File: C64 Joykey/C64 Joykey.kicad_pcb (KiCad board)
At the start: 2 copper layers, 99.7 x 74.9 mm, 30 parts, among them J1 Port_1, J2 Port_2, M1 Mounting, M2 Mounting, M3 Mounting, M4 Mounting, SW1 FIRE1, SW2 FIRE2, SW3 FIRE3, SW4 UP, SW5 DOWN, SW6 LEFT, SW7 RIGHT, SW8 RESET

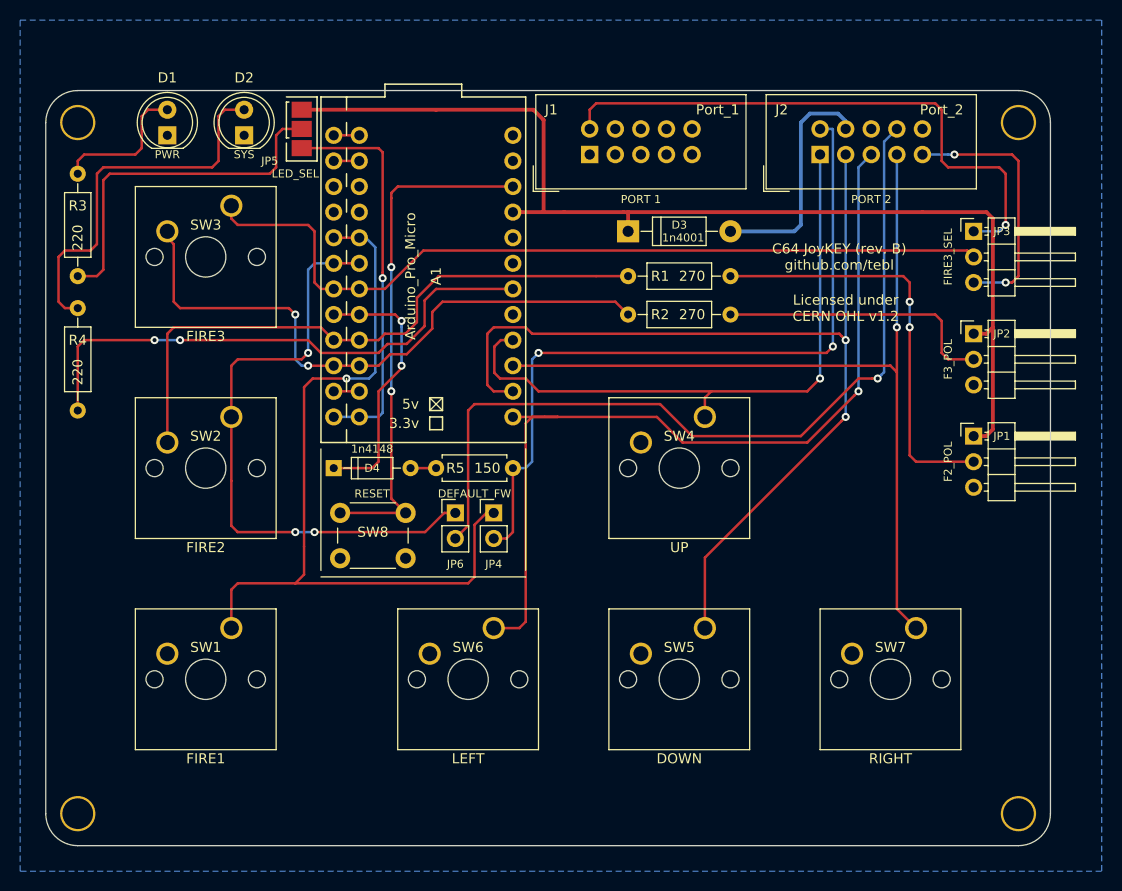
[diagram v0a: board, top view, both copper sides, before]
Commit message: Underglow LEDs added
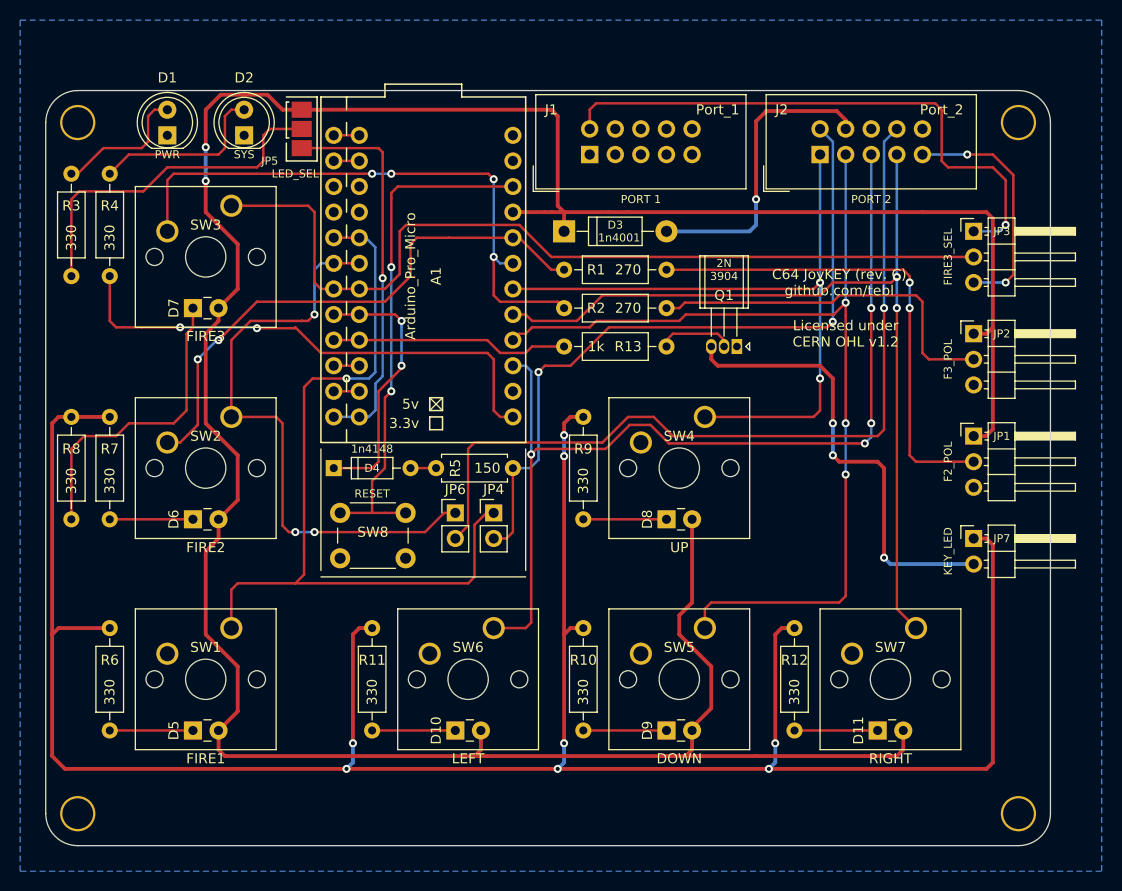
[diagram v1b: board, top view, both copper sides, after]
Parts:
- added D10: LED, LED_THT:LED_Rectangular_W3.0mm_H2.0mm, F.Cu at (181.6, 146.1)
- added D11: LED, LED_THT:LED_Rectangular_W3.0mm_H2.0mm, F.Cu at (223.5, 146.1)
- added D5: LED, LED_THT:LED_Rectangular_W3.0mm_H2.0mm, F.Cu at (155.6, 146.1)
- added D6: LED, LED_THT:LED_Rectangular_W3.0mm_H2.0mm, F.Cu at (155.6, 125.1)
- added D7: LED, LED_THT:LED_Rectangular_W3.0mm_H2.0mm, F.Cu at (155.6, 104.1)
- added D8: LED, LED_THT:LED_Rectangular_W3.0mm_H2.0mm, F.Cu at (202.6, 125.1)
- added D9: LED, LED_THT:LED_Rectangular_W3.0mm_H2.0mm, F.Cu at (202.6, 146.1)
- added JP7: KEY_LED, Connector_PinHeader_2.54mm:PinHeader_1x02_P2.54mm_Horizontal, F.Cu at (233.0, 127.0)
- added Q1: 2N3904, Package_TO_SOT_THT:TO-92_Inline_W4.0mm_Horizontal_FlatSideDown, F.Cu at (209.6, 108.0)
- added R10: 330, Resistor_THT:R_Axial_DIN0207_L6.3mm_D2.5mm_P10.16mm_Horizontal, F.Cu at (194.3, 146.1)
- added R11: 330, Resistor_THT:R_Axial_DIN0207_L6.3mm_D2.5mm_P10.16mm_Horizontal, F.Cu at (173.4, 146.1)
- added R12: 330, Resistor_THT:R_Axial_DIN0207_L6.3mm_D2.5mm_P10.16mm_Horizontal, F.Cu at (215.3, 146.1)
- added R13: 1k, Resistor_THT:R_Axial_DIN0207_L6.3mm_D2.5mm_P10.16mm_Horizontal, F.Cu at (202.6, 108.0)
- added R6: 330, Resistor_THT:R_Axial_DIN0207_L6.3mm_D2.5mm_P10.16mm_Horizontal, F.Cu at (147.3, 146.1)
- added R7: 330, Resistor_THT:R_Axial_DIN0207_L6.3mm_D2.5mm_P10.16mm_Horizontal, F.Cu at (147.3, 125.1)
- added R8: 330, Resistor_THT:R_Axial_DIN0207_L6.3mm_D2.5mm_P10.16mm_Horizontal, F.Cu at (143.5, 125.1)
- added R9: 330, Resistor_THT:R_Axial_DIN0207_L6.3mm_D2.5mm_P10.16mm_Horizontal, F.Cu at (194.3, 125.1)
- JP4, JP6: footprint Pin_Headers:Pin_Header_Straight_1x02_Pitch2.54mm -> Connector_PinHeader_2.54mm:PinHeader_1x02_P2.54mm_Vertical
- R1, R2: footprint Resistors_THT:R_Axial_DIN0207_L6.3mm_D2.5mm_P10.16mm_Horizontal -> Resistor_THT:R_Axial_DIN0207_L6.3mm_D2.5mm_P10.16mm_Horizontal
- R3, R4: value 220 -> 330; footprint Resistors_THT:R_Axial_DIN0207_L6.3mm_D2.5mm_P10.16mm_Horizontal -> Resistor_THT:R_Axial_DIN0207_L6.3mm_D2.5mm_P10.16mm_Horizontal
- R5: footprint Resistors_THT:R_Axial_DIN0207_L6.3mm_D2.5mm_P7.62mm_Horizontal -> Resistor_THT:R_Axial_DIN0207_L6.3mm_D2.5mm_P7.62mm_Horizontal
- moved R4 13.7 mm to (147.3, 90.8)
- moved R1 6.38 mm to (192.4, 100.3)
- moved R2 6.38 mm to (192.4, 104.1)
- moved D3 6.35 mm to (192.4, 96.5)
- moved R3 0.64 mm to (143.5, 90.8)
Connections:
- A1 pad 10: /FIRE3_POL -> Net-(A1-Pad10)
- A1 pad 13: P2_LEFT -> Net-(A1-Pad13)
- A1 pad 14: P2_DOWN -> Net-(A1-Pad14)
- A1 pad 15: P2_RIGHT -> P2_LEFT
- A1 pad 16: P2_UP -> P2_DOWN
- A1 pad 17: (no net) -> P2_RIGHT
- A1 pad 18: Net-(A1-Pad18) -> P2_UP
- A1 pad 19: (no net) -> FIRE3_POL
- A1 pad 20: (no net) -> FIRE2_POL
- A1 pad 24: (no net) -> Net-(A1-Pad24)
- A1 pad 9: /FIRE2_POL -> Net-(A1-Pad9)
- J1 pad 1: (no net) -> Net-(J1-Pad1)
- J1 pad 10: (no net) -> Net-(J1-Pad10)
- J1 pad 2: (no net) -> Net-(J1-Pad2)
- J1 pad 3: (no net) -> Net-(J1-Pad3)
- J1 pad 4: (no net) -> Net-(J1-Pad4)
- J1 pad 5: (no net) -> Net-(J1-Pad5)
- J1 pad 7: (no net) -> Net-(J1-Pad7)
- J1 pad 9: (no net) -> Net-(J1-Pad9)
- J2 pad 10: (no net) -> Net-(J2-Pad10)
- M1 pad 1: (no net) -> Net-(M1-Pad1)
- M2 pad 1: (no net) -> Net-(M2-Pad1)
- M3 pad 1: (no net) -> Net-(M3-Pad1)
- M4 pad 1: (no net) -> Net-(M4-Pad1)
- R1 pad 1: /FIRE2_POL -> FIRE2_POL
- R2 pad 1: /FIRE3_POL -> FIRE3_POL
- R4 pad 2: Net-(A1-Pad18) -> Net-(A1-Pad13)
- SW2 pad 2: /FIRE2_POL -> FIRE2_POL
- SW3 pad 2: /FIRE3_POL -> FIRE3_POL
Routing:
- net Net-(JP7-Pad1): track 0.00 -> 233.3 mm, vias 0 -> 8
- net VCC: track 108.6 -> 292.3 mm, vias 0 -> 2
- net /FIRE3_POL: track 61.7 -> 0.00 mm, vias 2 -> 0
- net /FIRE2_POL: track 61.3 -> 0.00 mm
- net FIRE3_POL: track 0.00 -> 59.2 mm, vias 0 -> 4
- net FIRE2_POL: track 0.00 -> 54.8 mm, vias 0 -> 2
- net Net-(A1-Pad18): track 54.4 -> 0.00 mm, vias 2 -> 0
- net Net-(A1-Pad13): track 0.00 -> 51.4 mm, vias 0 -> 2
- net Net-(JP7-Pad2): track 0.00 -> 45.4 mm, vias 0 -> 3
- net Net-(D7-Pad1): track 0.00 -> 30.4 mm
- net Net-(A1-Pad9): track 0.00 -> 24.3 mm
- net Net-(D2-Pad2): track 37.8 -> 17.8 mm
- net Net-(JP2-Pad2): track 27.8 -> 36.6 mm
- net Net-(D11-Pad1): track 0.00 -> 8.26 mm
- net Net-(D10-Pad1): track 0.00 -> 8.26 mm
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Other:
- rule pad_to_mask_clearance: 0.051 -> 0
- board text added: "2N 3904"
- board text added: "Amiga P1/P2 GND GND"
- board text added: "Atari P1 GND N/C"
- board text added: "Atari_7800* N/C N/C GND"
- board text added: "Atari_ST P1 GND GND"
- board text added: "C64 JoyKEY (rev. C) github.com/tebl"
- board text added: "C64(A) P1 GND VCC"
- board text added: "C64(B) P2 VCC VCC"
- board text added: "ENABLE"
- board text added: "FIRE3_SEL FIRE3_POL FIRE2_POL"
- board text added: "Install Arduino Pro Micro, if needed for USB function. Hold down LEFT + RIGHT key on powerup to enable. FIRE2/3 polarity must be set to GND, keys will be disabled in USB-mode if not."
- board text added: "KEY LED"
- board text added: "Kempston P2 GND GND"
- board text added: "SMS* N/C N/C GND"
- board text added: "Sinclair* N/C N/C N/C"
- board text added: "USB N/C GND GND"
- board text added: "~IMPORTANT! Configure FIRE2/FIRE3 polarity according to what the system required by the system, leave unjumpered (N/C) if you are not sure. You break it, you fix it!"
- board text removed: "Amiga GND GND"
- board text removed: "Atari N/C N/C"
- board text removed: "Atari_ST GND GND"
- board text removed: "C64 JoyKEY (rev. B) github.com/tebl"
- board text removed: "C64 VCC VCC"
- board text removed: "Install Arduino Pro Micro, if needed for USB function. Hold down LEFT + RIGHT key on powerup to enable. FIRE2/3 polarity must be set to GND, keys will be disabled USB-mode if not."
- board text removed: "Kempston GND GND"
- board text removed: "POLARITY P2 FIRE2 P2 FIRE3"
- board text removed: "PWR"
- board text removed: "SMS* GND N/C"
- board text removed: "SYS"
- board text removed: "USB GND GND"
- board text removed: "~IMPORTANT! Configure FIRE2/FIRE3 polarity according to what the system supports, or left unjumpered (N/C) just to be safe. Risk of harm to your system if not done correctly."

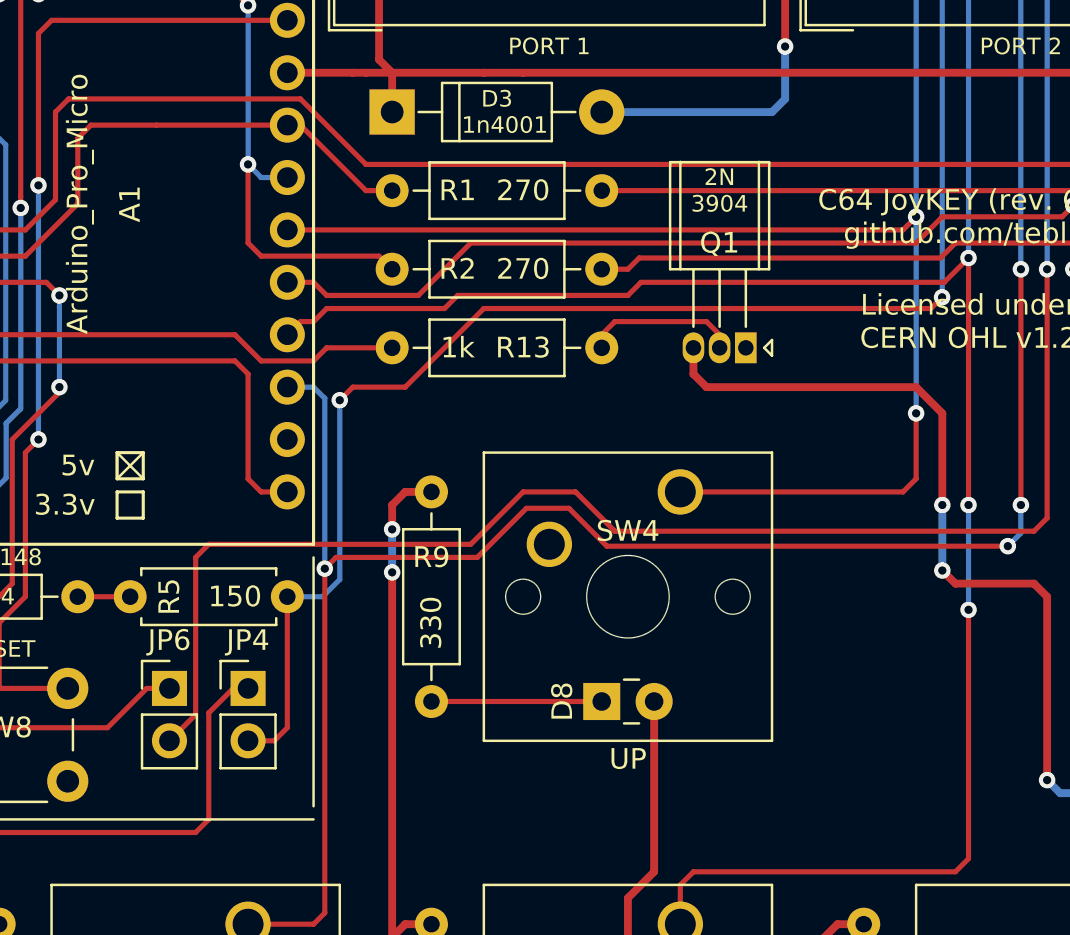
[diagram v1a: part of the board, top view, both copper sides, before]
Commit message: Changed Q1 footprint
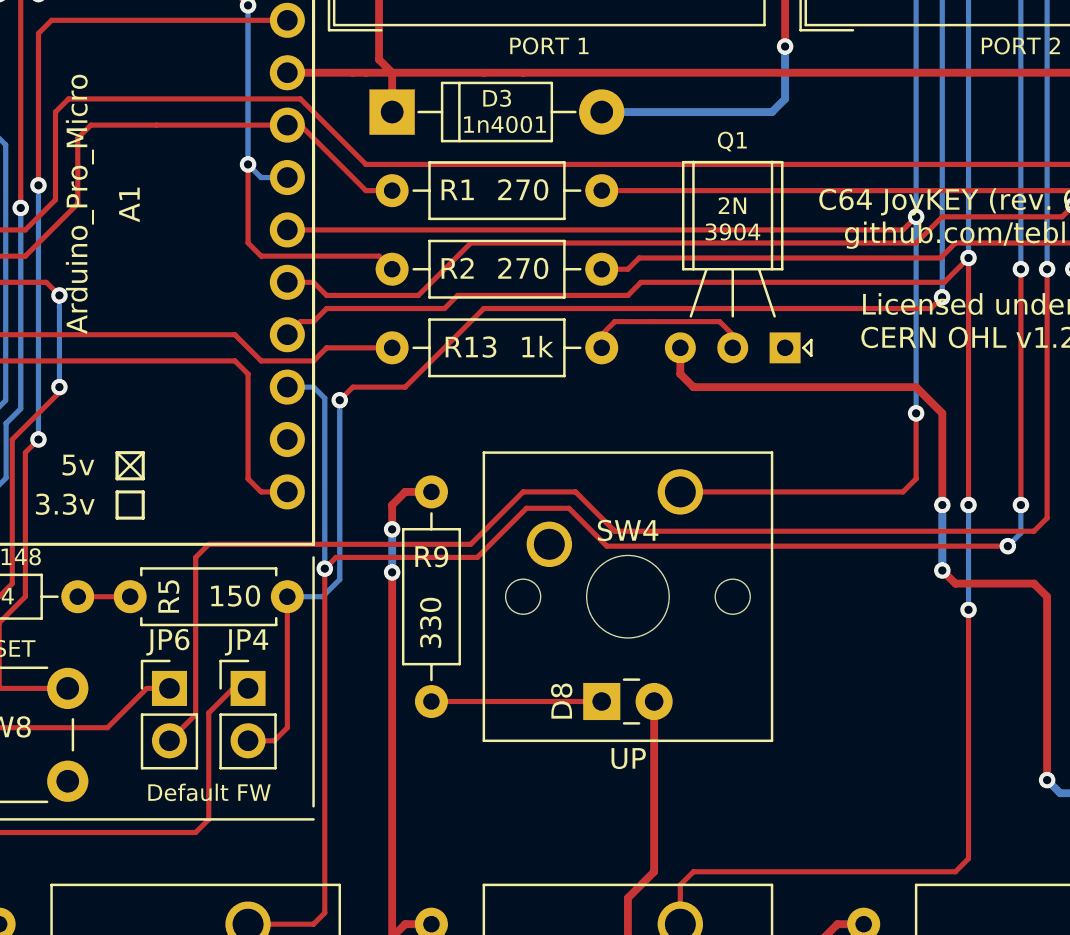
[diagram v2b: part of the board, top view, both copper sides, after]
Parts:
- Q1: footprint Package_TO_SOT_THT:TO-92_Inline_W4.0mm_Horizontal_FlatSideDown -> 2n3904:2N3904_TO-92_Horizontal_FlatSideDown
- moved Q1 0.63 mm to (210.2, 108.0)
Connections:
- A1 pad 14: Net-(A1-Pad14) -> (no net)
- A1 pad 24: Net-(A1-Pad24) -> (no net)
- J1 pad 1: Net-(J1-Pad1) -> (no net)
- J1 pad 10: Net-(J1-Pad10) -> (no net)
- J1 pad 2: Net-(J1-Pad2) -> (no net)
- J1 pad 3: Net-(J1-Pad3) -> (no net)
- J1 pad 4: Net-(J1-Pad4) -> (no net)
- J1 pad 5: Net-(J1-Pad5) -> (no net)
- J1 pad 7: Net-(J1-Pad7) -> (no net)
- J1 pad 9: Net-(J1-Pad9) -> (no net)
- J2 pad 10: Net-(J2-Pad10) -> (no net)
- M1 pad 1: Net-(M1-Pad1) -> (no net)
- M2 pad 1: Net-(M2-Pad1) -> (no net)
- M3 pad 1: Net-(M3-Pad1) -> (no net)
- M4 pad 1: Net-(M4-Pad1) -> (no net)
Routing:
- net Net-(JP7-Pad2): track 45.4 -> 46.0 mm
- net Net-(Q1-Pad2): track 7.51 -> 8.15 mm
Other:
- board text added: "Default FW"
- board text removed: "2N 3904"
